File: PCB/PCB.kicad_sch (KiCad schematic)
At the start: 61 parts, among them J1 Conn_01x02_Socket, J2 Conn_01x02_Pin, J3 Conn_01x02_Pin, J4 Conn_01x02_Socket, J5 Programming Pin, J6 Programming Pin, J7 Programming Pin, J8 Programming Pin, SW1 SW_Push, U1 STM32L476RGTx, U2 FGPMMOPA6H, U4 TPS63001DRCR, U5 LM2735XMF/NOPB, U8 LM386, U9 MAX7375AXR805

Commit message: Few more formatting things
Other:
- note added: "External Clock (Not in use)"
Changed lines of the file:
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@@
+		)
+	)
+	(text "External Clock (Not in use)\n"
+		(exclude_from_sim no)
+		(at 142.494 96.266 0)
+		(effects
+			(font
+				(size 0.508 0.508)
+			)
 		)
 	)

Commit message: pcb changes
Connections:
- net Debug 4: now reaches R9.2, U1.27 (PB1)
- net Debug 3: now reaches R8.2, U1.28 (PB2)
- net Debug 2: now reaches R7.2, U1.29 (PB10)
- net Debug 1: now reaches R6.2, U1.30 (PB11)
- net GPS RX: now reaches U1.42 (PA9), U2.P$10 (RX)
- net GPS TX: now reaches U1.43 (PA10), U2.P$9 (TX)
- net Clock: now reaches U1.5 (PH0), U9.2 (CLOCK)
- net LoRa RX: now reaches U1.53 (PC12), U3.3 (RXD)
- net LoRa TX: now reaches U1.54 (PD2), U3.4 (TXD)
- net Earth renamed GND
- net GND: now also U1.12 (VSSA); no longer C10.1, C13.1, C14.1, C15.1, C18.1, C19.1, C2.1, R4.1, U1.1 (VBAT), U1.19 (VDD), U1.32 (VDD), U1.48 (VDDUSB), U1.64 (VDD), U2.P$1 (VCC), U2.P$4 (VBACKUP), U3.1 (VDD), U3.2 (NRST), U4.1 (VOUT), U4.10 (FB), U9.1 (V+)
- net VDDA Connection renamed +3.3VADC
- net VDDA GND Connection: no longer names the net of C16.2, C17.2, R5.2
- net VDDA GND Connection: no longer U1.12 (VSSA)
- new net +3.3V: C10.1, C13.1, C14.1, C15.1, C18.1, C19.1, C2.1, R4.1, U1.1 (VBAT), U1.19 (VDD), U1.32 (VDD), U1.48 (VDDUSB), U1.64 (VDD), U2.P$1 (VCC), U2.P$4 (VBACKUP), U3.1 (VDD), U3.2 (NRST), U4.1 (VOUT), U4.10 (FB), U9.1 (V+)
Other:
- moved on the sheet: C18, C19, D2, D4, D5, D6, R6, R7, R8, R9, U2, U3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

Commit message: Schematic cleaned up
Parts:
- removed J5, J6, J7, J8: Programming Pin, symbol Connector_Generic_MountingPin:Conn_01x01_MountingPin
- removed R4, R5: 0 Ohms, symbol Device:R_US
- added R4, R5: 0 Ohm, Resistor_SMD:R_0805_2012Metric_Pad1.20x1.40mm_HandSolder, symbol Device:NetTie_2
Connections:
- net +3.3V: now also C20.1, SW1.2, U1.7 (NRST), R4.1
- net GND: now also C11.2, U8.3 (+), R5.1
- net Bat +: now reaches C1.1, C3.1, D1.1 (K), L2.1, R1.1, U4.5 (VIN), U4.6 (EN), U4.7 (PS_SYNC), U4.8 (VINA), U5.5 (VIN)
- net Bat +: no longer D3.2 (A), L2.2, U5.1 (SW)
- net DAC OUT: now reaches C11.1, U1.20 (PA4)
- net +5V: now reaches C12.1, C4.2, C5.1, D3.1 (K), R3.2, U8.6 (V+)
- net SWDIO: now reaches U1.46 (PA13)
- net SWCLK: now reaches U1.49 (PA14)
- net BOOT: now reaches U1.60 (BOOT0)
- net Amp Out: now reaches C8.1, C9.1, U8.5
- net Speaker: now reaches C9.2, J3.2 (Pin_2)
- net GNDA: now reaches C16.2, C17.2
- net GNDA: now also R5.2
- net - Amp: now reaches C7.1, U8.2 (-)
- net Bypass: now reaches C6.1, U8.7 (BYPASS)
- net +3.3VADC renamed 3.3VA
- net 3.3VA: now also R4.2
- new net: D3.2 (A), L2.2, U5.1 (SW)
- no-connect marks 57 -> 54
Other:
- moved on the sheet: C11, C12, C20, C3, C4, C5, C6, C7, C8, C9, D1, D2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

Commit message: pcb fix
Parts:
- removed H1, H2, H3, H4: MountingHole, symbol Mechanical:MountingHole
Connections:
- net Batteries: now reaches D1.2 (A), J2.2 (Pin_2)
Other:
- note added: "Amp"
- note added: "Debug LEDS"
- note added: "Ext Clock"
- note added: "GPS Chip"
- note added: "LoRa Chip"
- note added: "Reset Button"
- moved on the sheet: C11, C12, C18, C20, C6, C7, C8, C9, D1, SW1, U2, U3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

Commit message: minor pcb changes
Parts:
- added J5: Conn_01x04_Pin, symbol Connector:Conn_01x04_Pin
- added R10, R11: 100k Ohms, Resistor_SMD:R_0805_2012Metric, symbol Device:R_US
- C9: value 1000 uF -> 100 uF; footprint Polarized Cap 1000 uF:PCAP_10x10-ELECT_NCA -> Polarized Caps (.1 - 100 uF):CAP_UZE_4X3P9_NCH
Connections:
- net +3.3V: now also R11.2; no longer C20.1, SW1.2, U1.7 (NRST)
- net BOOT: now also R10.2
- net GND: now also J5.1 (Pin_1), R10.1; no longer U1.12 (VSSA)
- net GNDA: now also U1.12 (VSSA)
- net SWCLK: now also J5.2 (Pin_2)
- net SWDIO: now also J5.3 (Pin_3)
- new net RST: C20.1, J5.4 (Pin_4), R11.1, SW1.2, U1.7 (NRST)
- no-connect marks 54 -> 53
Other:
- note added: "Bootloader"
- note added: "Programming Pins"
- moved on the sheet: C20, SW1

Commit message: minor pcb tweaks
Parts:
- J5: footprint (none) -> Connector_JST:JST_EH_B4B-EH-A_1x04_P2.50mm_Vertical
- R1, R2, R3: footprint Resistor_SMD:R_0805_2012Metric -> Resistor_SMD:R_0805_2012Metric_Pad1.20x1.40mm_HandSolder
- U4: footprint Buck-Boost:DRC0010J -> Buck-Boost Converter Chip:DRC0010J
- U5: footprint Boost:MF05A -> Boost Converter Chip:MF05A
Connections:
- net SW Boost: now reaches D3.2 (A), L2.2, U5.1 (SW)
- net D4LED: now reaches D6.2 (A), R9.1
- net FB Boost: now reaches C4.1, R2.1, R3.1, U5.3 (FB)
- net D1LED: now reaches D2.2 (A), R6.1
- net D3LED: now reaches D5.2 (A), R8.1
- net EN Boost: now reaches R1.2, U5.4 (EN)
- net D2LED: now reaches D4.2 (A), R7.1
- net L2 Buck: now reaches L1.2, U4.2 (L2)
- net L1 Buck: now reaches L1.1, U4.4 (L1)
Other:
- moved on the sheet: D2, D4, D5, D6

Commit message: Add files via upload
Finished PCB, awaiting check from professor and TAs
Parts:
- added H1, H2, H3, H4: MountingHole, MountingHole:MountingHole_2.1mm, symbol Mechanical:MountingHole
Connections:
- net Debug 1: now also U1.36 (PB15); no longer U1.30 (PB11)
- net Debug 2: now also U1.34 (PB13); no longer U1.29 (PB10)
- net Debug 3: now also U1.35 (PB14); no longer U1.28 (PB2)
- net Debug 4: now also U1.33 (PB12); no longer U1.27 (PB1)
- net LoRa RX: now also U1.24 (PC4); no longer U1.53 (PC12)
- net LoRa TX: now also U1.25 (PC5); no longer U1.54 (PD2)

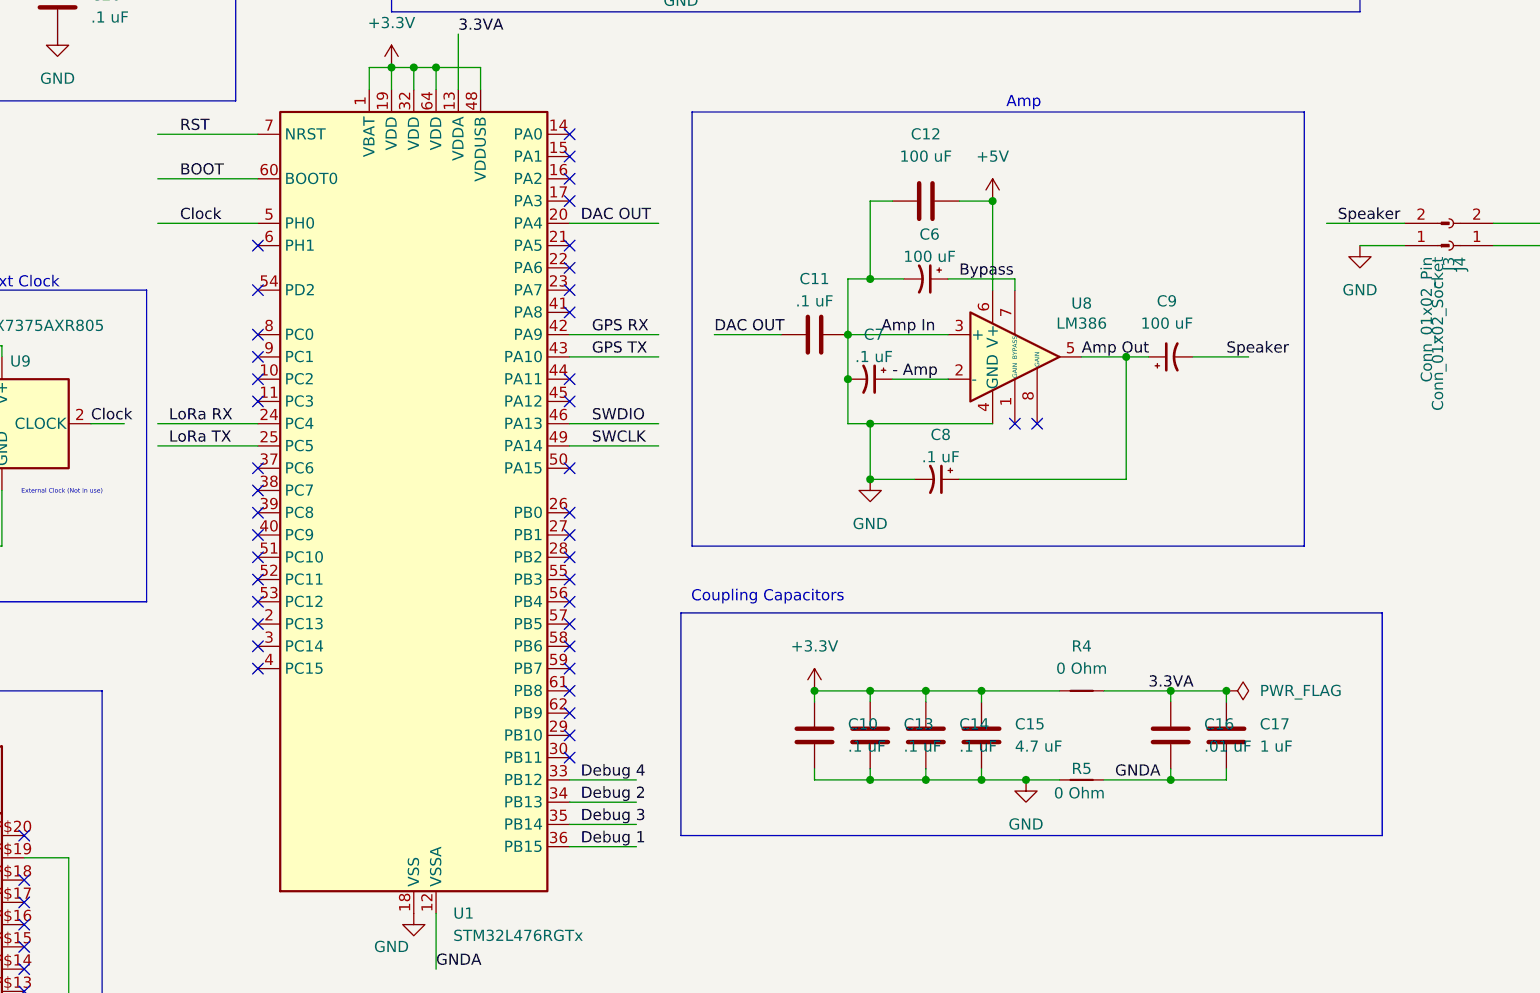
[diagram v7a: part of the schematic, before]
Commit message: Debug vias added
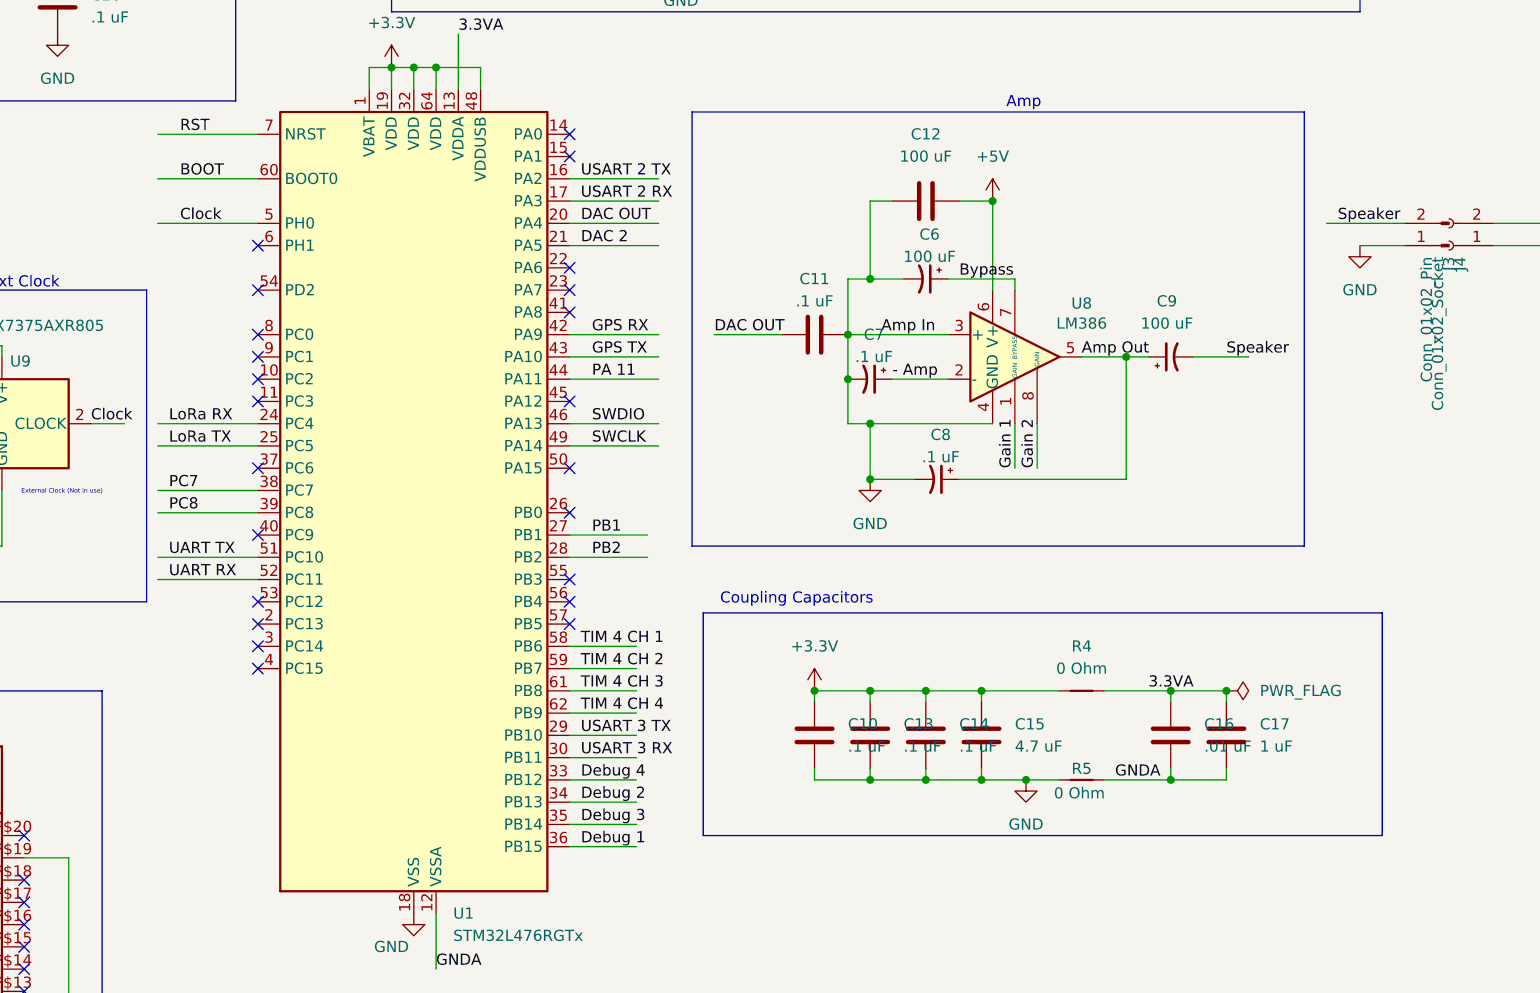
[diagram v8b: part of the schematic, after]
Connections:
- net USART 2 TX: now reaches U1.16 (PA2)
- net USART 2 RX: now reaches U1.17 (PA3)
- net DAC 2: now reaches U1.21 (PA5)
- net PB1: now reaches U1.27 (PB1)
- net PB2: now reaches U1.28 (PB2)
- net USART 3 TX: now reaches U1.29 (PB10)
- net USART 3 RX: now reaches U1.30 (PB11)
- net PC7: now reaches U1.38 (PC7)
- net PC8: now reaches U1.39 (PC8)
- net PA 11: now reaches U1.44 (PA11)
- net UART TX: now reaches U1.51 (PC10)
- net UART RX: now reaches U1.52 (PC11)
- net TIM 4 CH 1: now reaches U1.58 (PB6)
- net TIM 4 CH 2: now reaches U1.59 (PB7)
- net TIM 4 CH 3: now reaches U1.61 (PB8)
- net TIM 4 CH 4: now reaches U1.62 (PB9)
- net Gain 1: now reaches U8.1 (GAIN)
- net Gain 2: now reaches U8.8 (GAIN)
- no-connect marks 53 -> 35
